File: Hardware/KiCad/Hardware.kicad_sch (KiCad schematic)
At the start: 1 part, among them U2 Teensy4.1

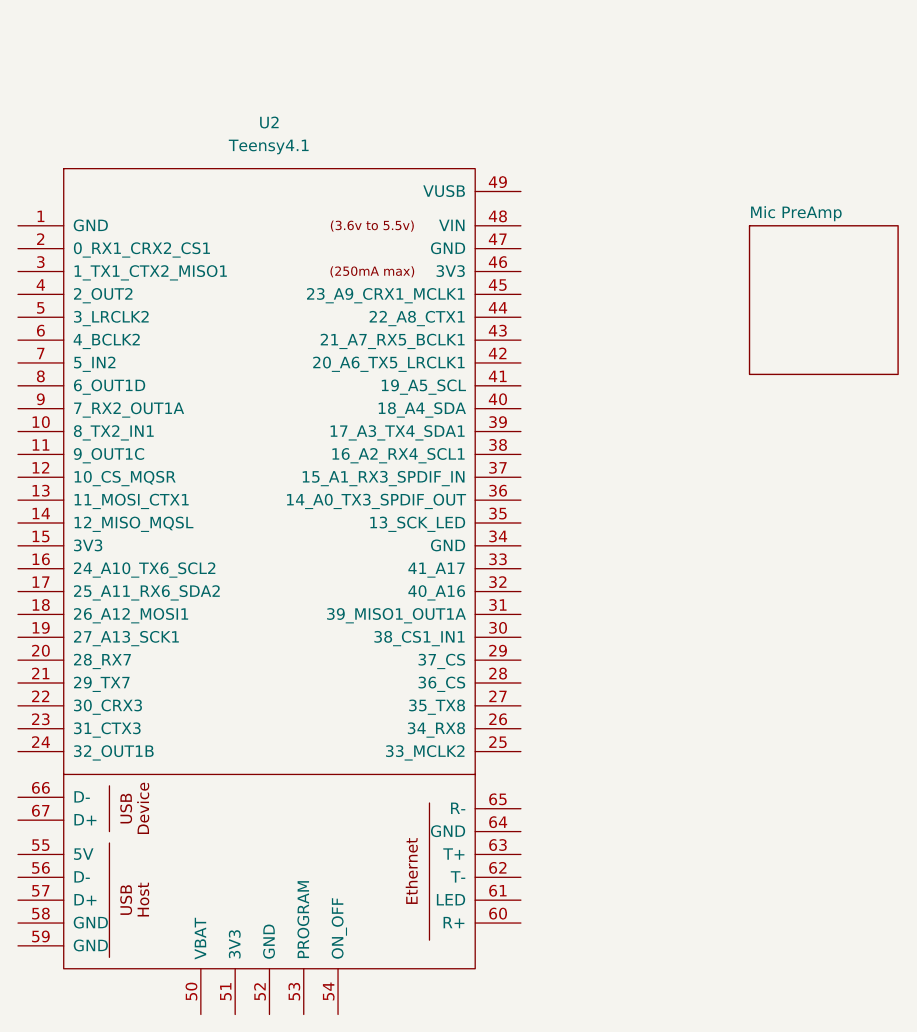
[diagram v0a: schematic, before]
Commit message: Hierarchical sheet for MCU
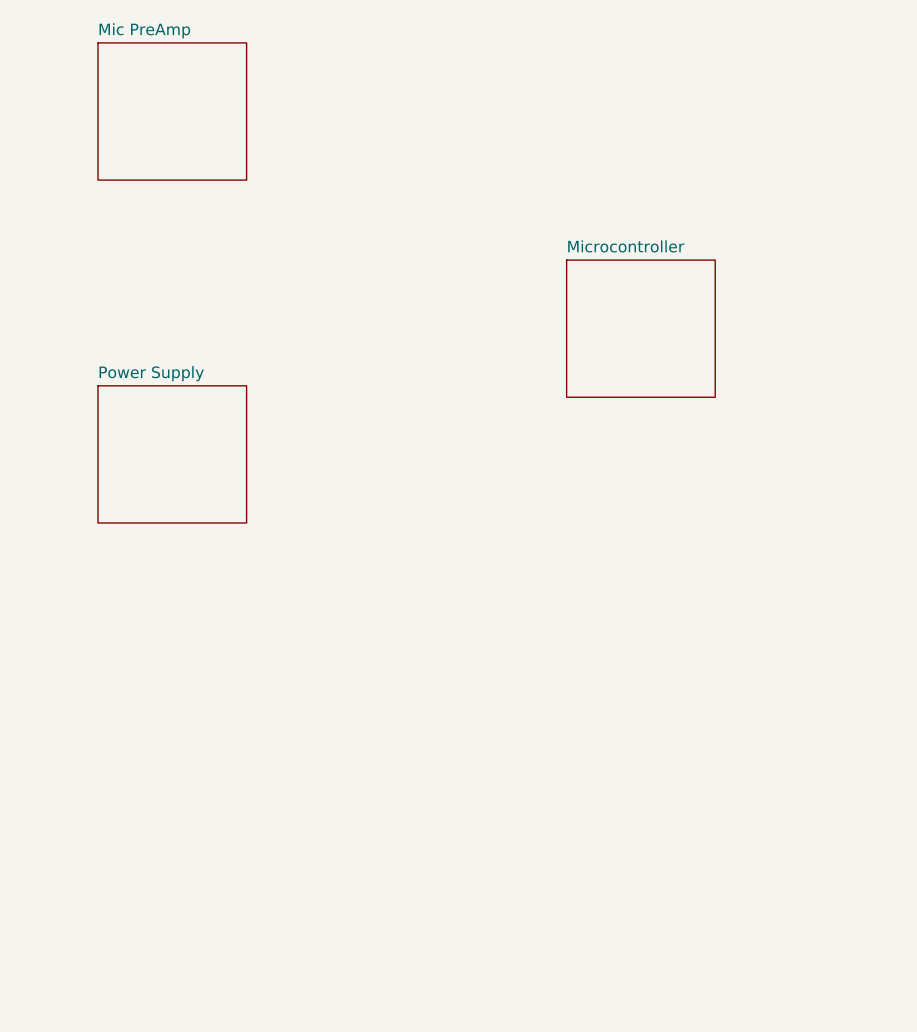
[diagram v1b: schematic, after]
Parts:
- removed U2: Teensy4.1, symbol Teensy:Teensy4.1
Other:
- added sheet Microcontroller (MCU.kicad_sch)
- added sheet Power Supply (PSU.kicad_sch)
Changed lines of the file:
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@@
 		(comment 1 "Tim Wannet")
 	)
-	(symbol
-		(lib_id "Teensy:Teensy4.1")
-		(at 69.85 123.19 0)
-		(unit 1)
-		(exclude_from_sim no)
-		(in_bom yes)
-		(on_board yes)
-		(dnp no)
-		(fields_autoplaced yes)
-		(property "Reference" "U2"
-			(at 69.85 57.15 0)
-			(effects
-				(font
-					(size 1.27 1.27)
-				)
-			)
-		)
-		(property "Value" "Teensy4.1"
-			(at 69.85 59.69 0)
-			(effects
-				(font
-					(size 1.27 1.27)
-				)
-			)
-		)
-		(property "Footprint" ""
-			(at 59.69 113.03 0)
-			(effects
-				(font
-					(size 1.27 1.27)
-				)
-				(hide yes)
-			)
-		)
-		(property "Datasheet" ""
-			(at 59.69 113.03 0)
-			(effects
-				(font
-					(size 1.27 1.27)
-				)
-				(hide yes)
-			)
-		)
-		(property "Description" ""
-			(at 69.85 123.19 0)
-			(effects
-				(font
-					(size 1.27 1.27)
-				)
-				(hide yes)
-			)
-		)
-		(pin "23"
-		)
-		(pin "58"
-		)
-		(pin "65"
-		)
-		(pin "35"
-		)
-		(pin "12"
-		)
-		(pin "11"
-		)
-		(pin "2"
-		)
-		(pin "29"
-		)
-		(pin "18"
-		)
-		(pin "15"
-		)
-		(pin "46"
-		)
-		(pin "48"
-		)
-		(pin "22"
-		)
-		(pin "47"
-		)
-		(pin "55"
-		)
-		(pin "52"
-		)
-		(pin "36"
-		)
-		(pin "57"
-		)
-		(pin "24"
-		)
-		(pin "31"
-		)
-		(pin "28"
-		)
-		(pin "30"
-		)
-		(pin "49"
-		)
-		(pin "20"
-		)
-		(pin "51"
-		)
-		(pin "40"
-		)
-		(pin "67"
-		)
-		(pin "17"
-		)
-		(pin "19"
-		)
-		(pin "13"
-		)
-		(pin "63"
-		)
-		(pin "64"
-		)
-		(pin "26"
-		)
-		(pin "1"
-		)
-		(pin "21"
-		)
-		(pin "44"
-		)
-		(pin "42"
-		)
-		(pin "37"
-		)
-		(pin "45"
-		)
-		(pin "3"
-		)
-		(pin "43"
-		)
-		(pin "7"
-		)
-		(pin "5"
-		)
-		(pin "10"
-		)
-		(pin "41"
-		)
-		(pin "38"
-		)
-		(pin "39"
-		)
-		(pin "33"
-		)
-		(pin "34"
-		)
-		(pin "50"
-		)
-		(pin "4"
-		)
-		(pin "27"
-		)
-		(pin "53"
-		)
-		(pin "14"
-		)
-		(pin "62"
-		)
-		(pin "9"
-		)
-		(pin "8"
-		)
-		(pin "56"
-		)
-		(pin "16"
-		)
-		(pin "32"
-		)
-		(pin "54"
-		)
-		(pin "59"
-		)
-		(pin "6"
-		)
-		(pin "61"
-		)
-		(pin "60"
-		)
-		(pin "25"
-		)
-		(pin "66"
-		)
-		(instances
-			(project ""
-				(path "/e827c80a-ca8d-4d24-8db6-878b575a1aed"
-					(reference "U2")
-					(unit 1)
-				)
-			)
-		)
-	)
 	(sheet
-		(at 123.19 68.58)
-		(size 16.51 16.51)
+		(at 102.87 72.39)
+		(size 16.51 15.24)
 		(fields_autoplaced yes)
 		(stroke
@@
 			(color 0 0 0 0.0000)
 		)
-		(property "Sheetname" "Mic PreAmp"
-			(at 123.19 67.8684 0)
-			(show_name yes)
+		(property "Sheetname" "Microcontroller"
+			(at 102.87 71.6784 0)
 			(effects
 				(font
@@
 			)
 		)
-		(property "Sheetfile" "PreAmp.kicad_sch"
-			(at 123.19 85.6746 0)
+		(property "Sheetfile" "MCU.kicad_sch"
+			(at 102.87 88.2146 0)
+			(effects
+				(font
+					(size 1.27 1.27)
+				)
+				(justify left top)
+				(hide yes)
+			)
+		)
+		(instances
+			(project "Hardware"
+				(path "/e827c80a-ca8d-4d24-8db6-878b575a1aed"
+					(page "3")
+				)
+			)
+		)
+	)
+	(sheet
+		(at 50.8 86.36)
+		(size 16.51 15.24)
+		(fields_autoplaced yes)
+		(stroke
+			(width 0.1524)
+			(type solid)
+		)
+		(fill
+			(color 0 0 0 0.0000)
+		)
+		(property "Sheetname" "Power Supply"
+			(at 50.8 85.6484 0)
+			(effects
+				(font
+					(size 1.27 1.27)
+				)
+				(justify left bottom)
+			)
+		)
+		(property "Sheetfile" "PSU.kicad_sch"
+			(at 50.8 102.1846 0)
 			(effects
 				(font
@@
 				)
 			)
+		)
+	)
+	(sheet
+		(at 50.8 48.26)
+		(size 16.51 15.24)
+		(fields_autoplaced yes)
+		(stroke
+			(width 0.1524)
+			(type solid)
+		)
+		(fill
+			(color 0 0 0 0.0000)
+		)
+		(property "Sheetname" "Mic PreAmp"
+			(at 50.8 47.5484 0)
+			(show_name yes)
+			(effects
+				(font
+					(size 1.27 1.27)
+				)
+				(justify left bottom)
+			)
+		)
+		(property "Sheetfile" "PreAmp.kicad_sch"
+			(at 50.8 64.0846 0)
+			(effects
+				(font
+					(size 1.27 1.27)
+				)
+				(justify left top)
+				(hide yes)
+			)
+		)
+		(instances
+			(project "Hardware"
+				(path "/e827c80a-ca8d-4d24-8db6-878b575a1aed"
+					(page "4")
+				)
+			)

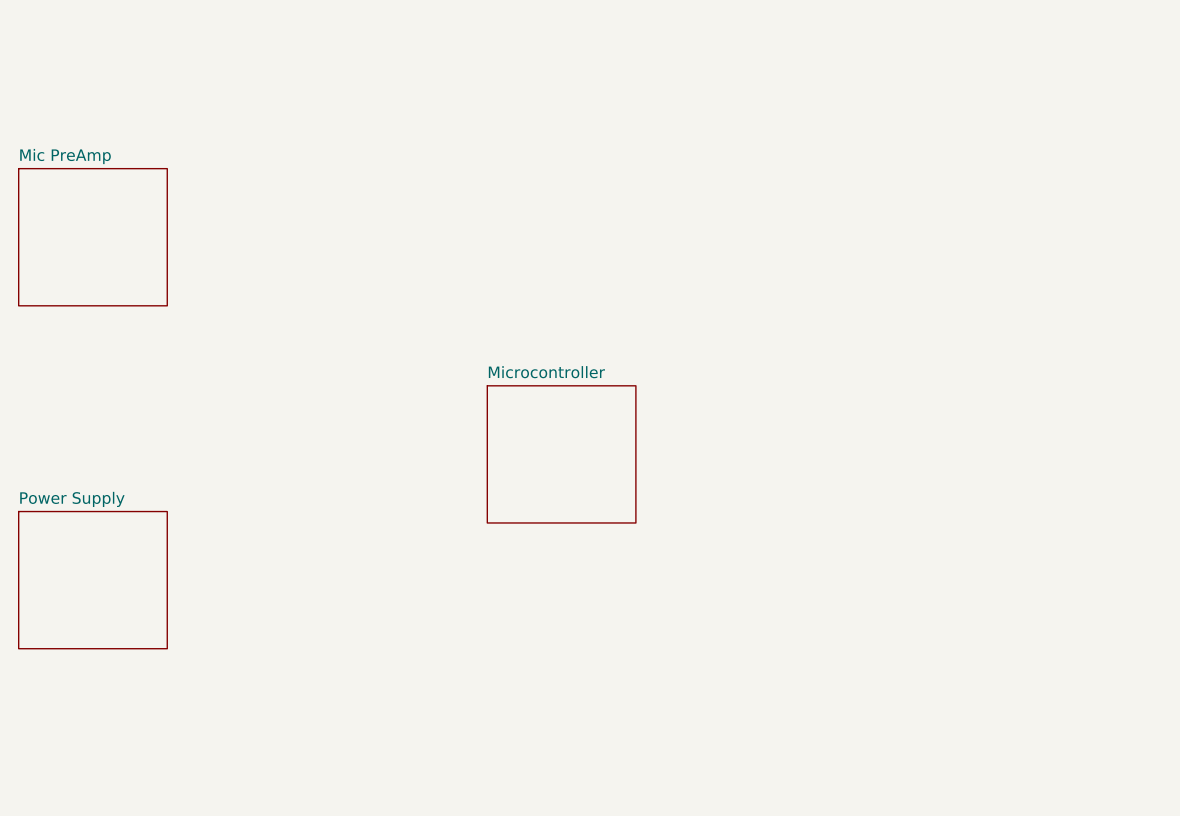
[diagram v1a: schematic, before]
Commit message: Midi in circuit with optocoupler and  isolation/input protection
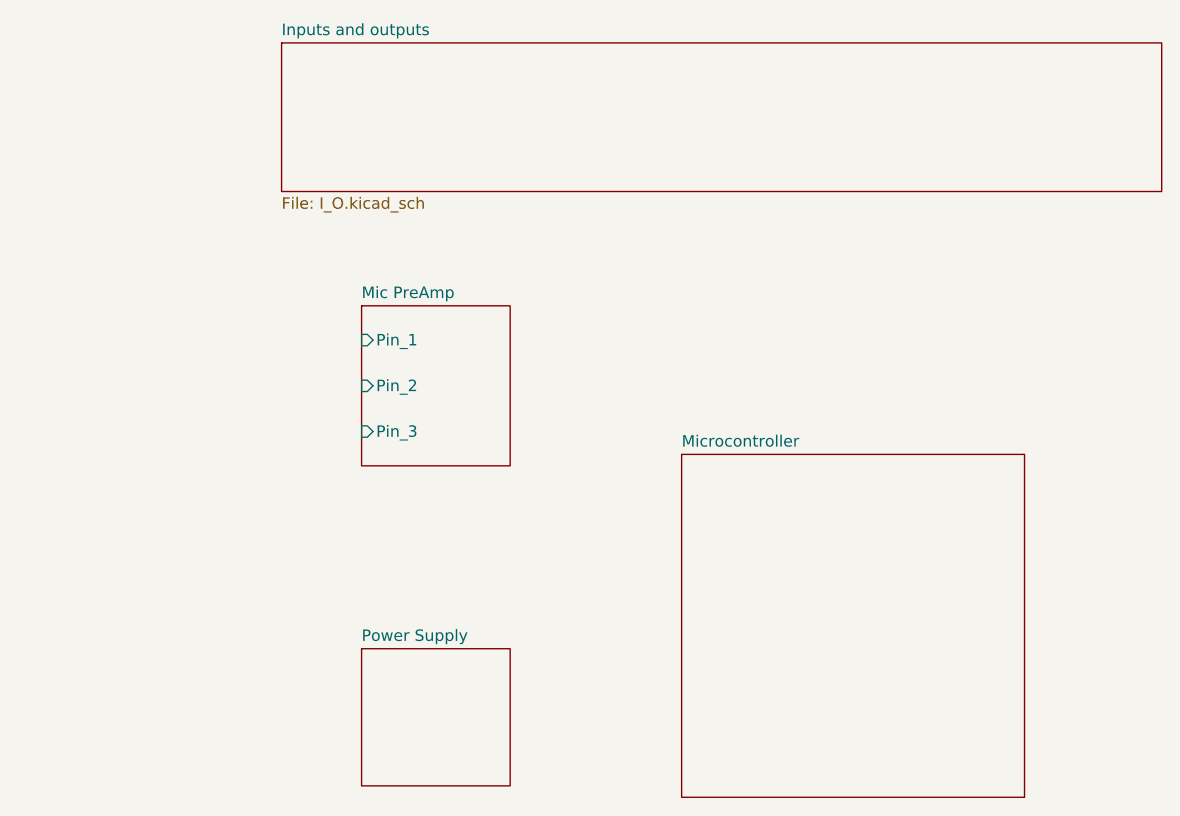
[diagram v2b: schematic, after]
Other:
- added sheet Inputs and outputs (I_O.kicad_sch)
- sheet Mic PreAmp ports: added Pin_1, Pin_2, Pin_3; removed none
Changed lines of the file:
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@@
 (kicad_sch
-	(version 20231120)
+	(version 20250114)
 	(generator "eeschema")
-	(generator_version "8.0")
+	(generator_version "9.0")
 	(paper "A4")
 	(title_block
@@
 	)
 	(sheet
-		(at 102.87 72.39)
+		(at 124.46 80.01)
+		(size 38.1 38.1)
+		(exclude_from_sim no)
+		(in_bom yes)
+		(on_board yes)
+		(dnp no)
+		(fields_autoplaced yes)
+		(stroke
+			(width 0.1524)
+			(type solid)
+		)
+		(fill
+			(color 0 0 0 0.0000)
+		)
+		(property "Sheetname" "Microcontroller"
+			(at 124.46 79.2984 0)
+			(effects
+				(font
+					(size 1.27 1.27)
+				)
+				(justify left bottom)
+			)
+		)
+		(property "Sheetfile" "MCU.kicad_sch"
+			(at 124.46 118.6946 0)
+			(effects
+				(font
+					(size 1.27 1.27)
+				)
+				(justify left top)
+				(hide yes)
+			)
+		)
+		(instances
+			(project "Hardware"
+				(path "/e827c80a-ca8d-4d24-8db6-878b575a1aed"
+					(page "3")
+				)
+			)
+		)
+	)
+	(sheet
+		(at 80.01 34.29)
+		(size 97.79 16.51)
+		(exclude_from_sim no)
+		(in_bom yes)
+		(on_board yes)
+		(dnp no)
+		(fields_autoplaced yes)
+		(stroke
+			(width 0.1524)
+			(type solid)
+		)
+		(fill
+			(color 0 0 0 0.0000)
+		)
+		(property "Sheetname" "Inputs and outputs"
+			(at 80.01 33.5784 0)
+			(effects
+				(font
+					(size 1.27 1.27)
+				)
+				(justify left bottom)
+			)
+		)
+		(property "Sheetfile" "I_O.kicad_sch"
+			(at 80.01 51.3846 0)
+			(effects
+				(font
+					(size 1.27 1.27)
+				)
+				(justify left top)
+			)
+		)
+		(instances
+			(project "Hardware"
+				(path "/e827c80a-ca8d-4d24-8db6-878b575a1aed"
+					(page "5")
+				)
+			)
+		)
+	)
+	(sheet
+		(at 88.9 101.6)
 		(size 16.51 15.24)
-		(fields_autoplaced yes)
-		(stroke
-			(width 0.1524)
-			(type solid)
-		)
-		(fill
-			(color 0 0 0 0.0000)
-		)
-		(property "Sheetname" "Microcontroller"
-			(at 102.87 71.6784 0)
-			(effects
-				(font
-					(size 1.27 1.27)
-				)
-				(justify left bottom)
-			)
-		)
-		(property "Sheetfile" "MCU.kicad_sch"
-			(at 102.87 88.2146 0)
+		(exclude_from_sim no)
+		(in_bom yes)
+		(on_board yes)
+		(dnp no)
+		(fields_autoplaced yes)
+		(stroke
+			(width 0.1524)
+			(type solid)
+		)
+		(fill
+			(color 0 0 0 0.0000)
+		)
+		(property "Sheetname" "Power Supply"
+			(at 88.9 100.8884 0)
+			(effects
+				(font
+					(size 1.27 1.27)
+				)
+				(justify left bottom)
+			)
+		)
+		(property "Sheetfile" "PSU.kicad_sch"
+			(at 88.9 117.4246 0)
 			(effects
 				(font
@@
 			(project "Hardware"
 				(path "/e827c80a-ca8d-4d24-8db6-878b575a1aed"
-					(page "3")
-				)
-			)
-		)
-	)
-	(sheet
-		(at 50.8 86.36)
-		(size 16.51 15.24)
-		(fields_autoplaced yes)
-		(stroke
-			(width 0.1524)
-			(type solid)
-		)
-		(fill
-			(color 0 0 0 0.0000)
-		)
-		(property "Sheetname" "Power Supply"
-			(at 50.8 85.6484 0)
-			(effects
-				(font
-					(size 1.27 1.27)
-				)
-				(justify left bottom)
-			)
-		)
-		(property "Sheetfile" "PSU.kicad_sch"
-			(at 50.8 102.1846 0)
+					(page "2")
+				)
+			)
+		)
+	)
+	(sheet
+		(at 88.9 63.5)
+		(size 16.51 17.78)
+		(exclude_from_sim no)
+		(in_bom yes)
+		(on_board yes)
+		(dnp no)
+		(fields_autoplaced yes)
+		(stroke
+			(width 0.1524)
+			(type solid)
+		)
+		(fill
+			(color 0 0 0 0.0000)
+		)
+		(property "Sheetname" "Mic PreAmp"
+			(at 88.9 62.7884 0)
+			(effects
+				(font
+					(size 1.27 1.27)
+				)
+				(justify left bottom)
+			)
+		)
+		(property "Sheetfile" "PreAmp.kicad_sch"
+			(at 88.9 81.8646 0)
 			(effects
 				(font
@@
 			)
 		)
-		(instances
-			(project "Hardware"
-				(path "/e827c80a-ca8d-4d24-8db6-878b575a1aed"
-					(page "2")
-				)
-			)
-		)
-	)
-	(sheet
-		(at 50.8 48.26)
-		(size 16.51 15.24)
-		(fields_autoplaced yes)
-		(stroke
-			(width 0.1524)
-			(type solid)
-		)
-		(fill
-			(color 0 0 0 0.0000)
-		)
-		(property "Sheetname" "Mic PreAmp"
-			(at 50.8 47.5484 0)
-			(show_name yes)
-			(effects
-				(font
-					(size 1.27 1.27)
-				)
-				(justify left bottom)
-			)
-		)
-		(property "Sheetfile" "PreAmp.kicad_sch"
-			(at 50.8 64.0846 0)
-			(effects
-				(font
-					(size 1.27 1.27)
-				)
-				(justify left top)
-				(hide yes)
+		(pin "Pin_1" input
+			(at 88.9 67.31 180)
+			(effects
+				(font
+					(size 1.27 1.27)
+				)
+				(justify left)
+			)
+		)
+		(pin "Pin_2" input
+			(at 88.9 72.39 180)
+			(effects
+				(font
+					(size 1.27 1.27)
+				)
+				(justify left)
+			)
+		)
+		(pin "Pin_3" input
+			(at 88.9 77.47 180)
+			(effects
+				(font
+					(size 1.27 1.27)
+				)
+				(justify left)
 			)
 		)
@@
 		)
 	)
+	(embedded_fonts no)
 )

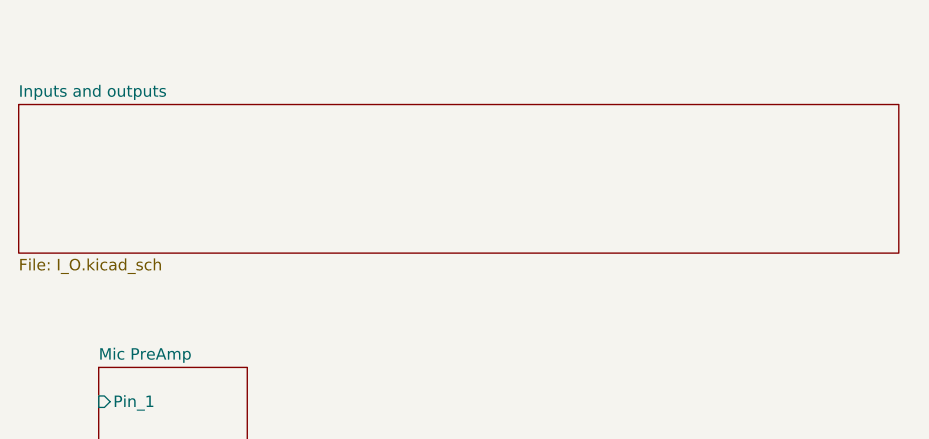
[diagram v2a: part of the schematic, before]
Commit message: Labeled, sheet out from modulator
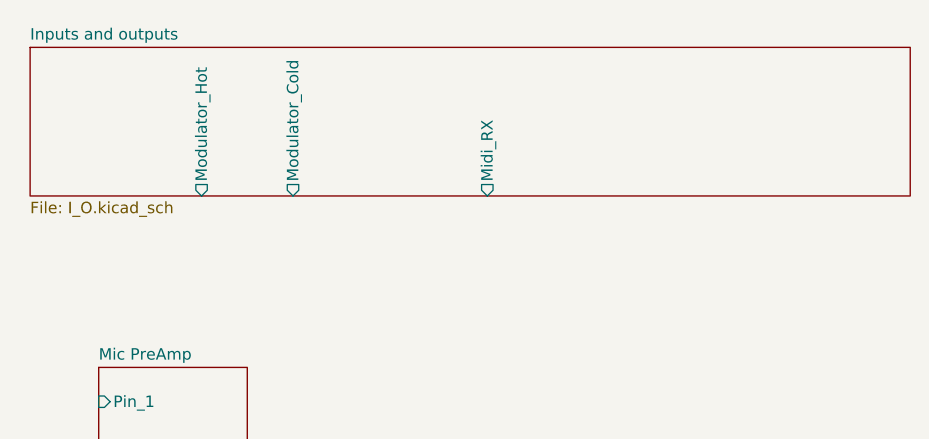
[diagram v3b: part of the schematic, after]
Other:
- sheet Inputs and outputs ports: added Midi_RX, Modulator_Cold, Modulator_Hot; removed none
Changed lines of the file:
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@@
 	)
 	(sheet
-		(at 80.01 34.29)
+		(at 81.28 27.94)
 		(size 97.79 16.51)
 		(exclude_from_sim no)
@@
 		)
 		(property "Sheetname" "Inputs and outputs"
-			(at 80.01 33.5784 0)
+			(at 81.28 27.2284 0)
 			(effects
 				(font
@@
 		)
 		(property "Sheetfile" "I_O.kicad_sch"
-			(at 80.01 51.3846 0)
+			(at 81.28 45.0346 0)
 			(effects
 				(font
@@
 			)
 		)
+		(pin "Midi_RX" output
+			(at 132.08 44.45 270)
+			(effects
+				(font
+					(size 1.27 1.27)
+				)
+				(justify left)
+			)
+		)
+		(pin "Modulator_Cold" output
+			(at 110.49 44.45 270)
+			(effects
+				(font
+					(size 1.27 1.27)
+				)
+				(justify left)
+			)
+		)
+		(pin "Modulator_Hot" output
+			(at 100.33 44.45 270)
+			(effects
+				(font
+					(size 1.27 1.27)
+				)
+				(justify left)
+			)
+		)
